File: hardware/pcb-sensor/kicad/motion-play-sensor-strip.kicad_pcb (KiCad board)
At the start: 2 copper layers, 69.8 x 10 mm, 9 parts, among them J1 Power In, J2 Power Out, J3 I2C+INT, U1 VCNL4040M3OE-H3

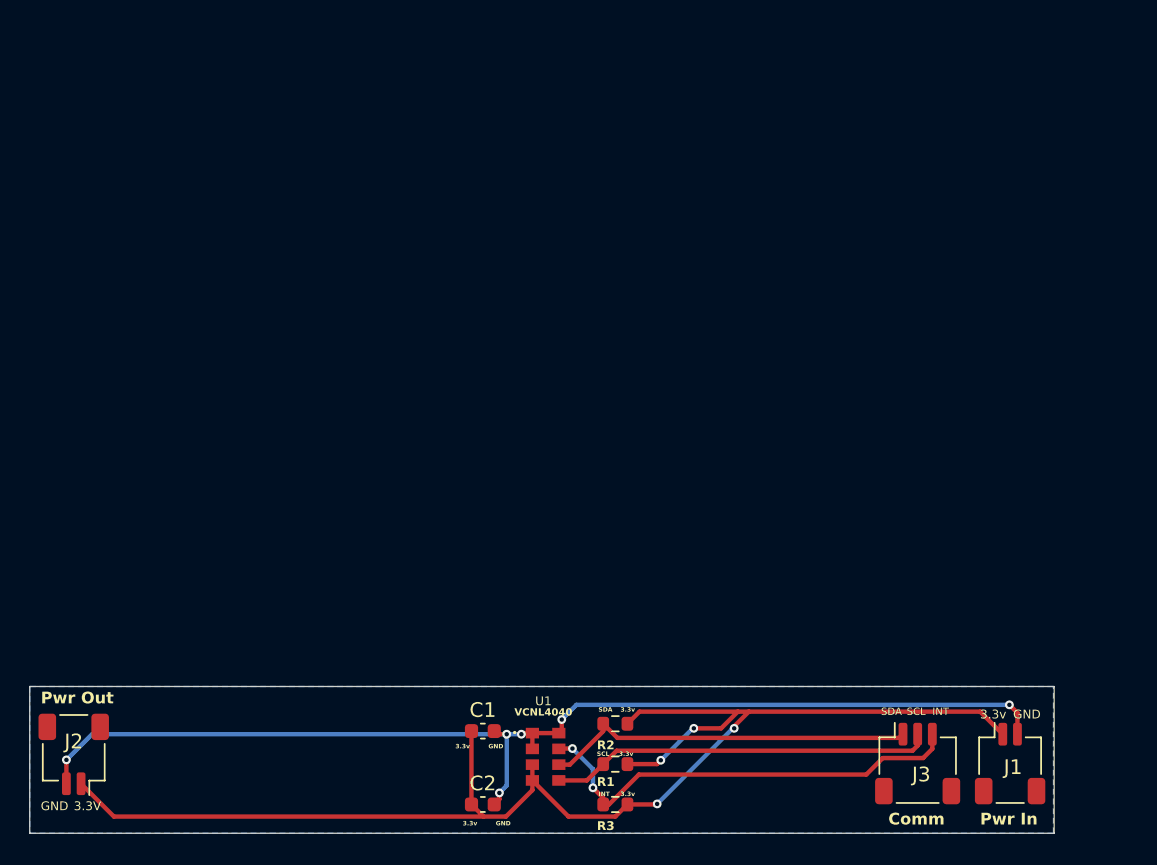
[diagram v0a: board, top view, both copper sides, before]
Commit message: Finished sensor redesign
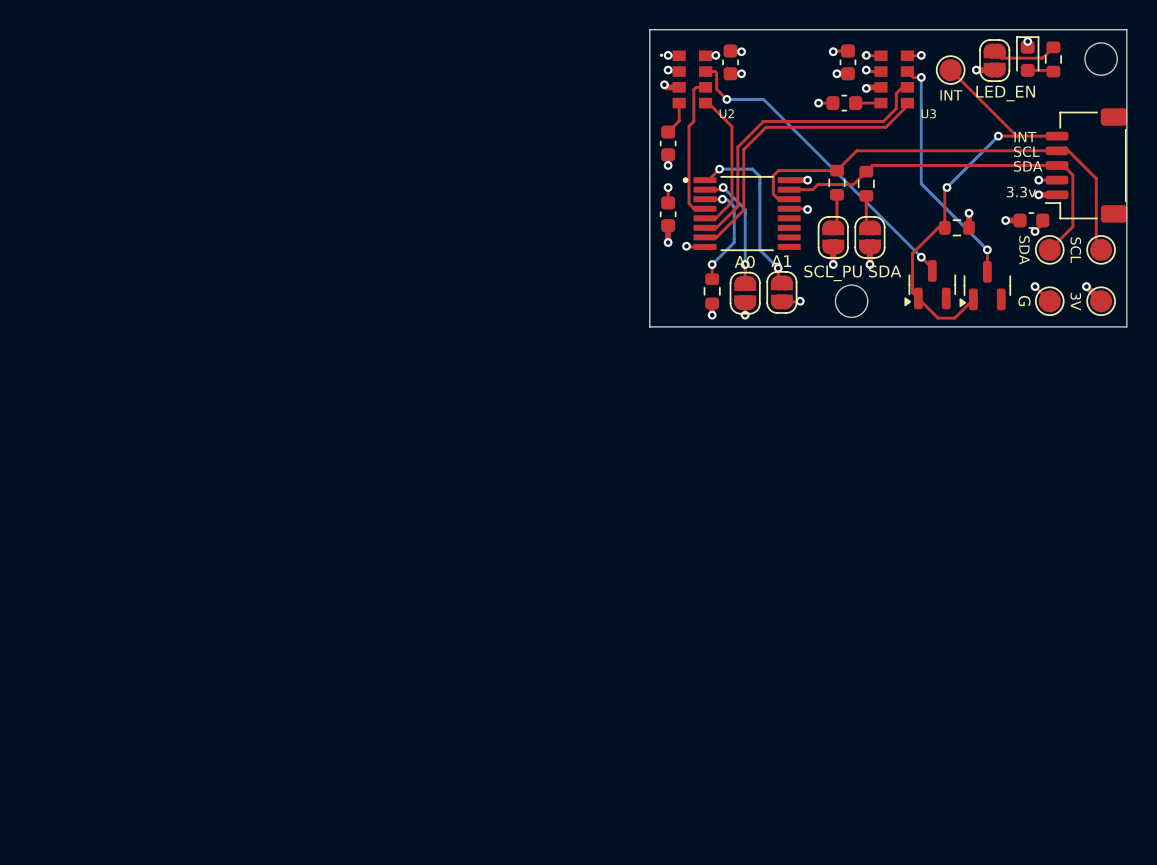
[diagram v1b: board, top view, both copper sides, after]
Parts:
- removed J2: Power Out, Connector_JST:JST_SH_SM02B-SRSS-TB_1x02-1MP_P1.00mm_Horizontal
- removed J3: I2C+INT, Connector_JST:JST_SH_SM03B-SRSS-TB_1x03-1MP_P1.00mm_Horizontal
- added C3: 2.2µF, Capacitor_SMD:C_0603_1608Metric, F.Cu at (143.5, 56.0)
- added C4: 2.2µF, Capacitor_SMD:C_0603_1608Metric, F.Cu at (155.5, 53.2)
- added C5: 0.1µF, Capacitor_SMD:C_0603_1608Metric, F.Cu at (155.8, 50.5)
- added C6: 0.1µF, Capacitor_SMD:C_0603_1608Metric, F.Cu at (143.5, 60.8)
- added D1: LED, LED_SMD:LED_0603_1608Metric, F.Cu at (168.0, 50.2)
- added D2: BAT54S, Package_TO_SOT_SMD:SOT-23, F.Cu at (161.5, 65.6)
- added D3: BAT54S, Package_TO_SOT_SMD:SOT-23, F.Cu at (165.2, 65.7)
- added JP1: SolderJumper_2_Open, Jumper:SolderJumper-2_P1.3mm_Open_RoundedPad1.0x1.5mm, F.Cu at (157.2, 62.4)
- added JP2: SolderJumper_2_Open, Jumper:SolderJumper-2_P1.3mm_Open_RoundedPad1.0x1.5mm, F.Cu at (154.8, 62.4)
- added JP3: SolderJumper_2_Open, Jumper:SolderJumper-2_P1.3mm_Open_RoundedPad1.0x1.5mm, F.Cu at (148.8, 66.2)
- added JP4: SolderJumper_2_Open, Jumper:SolderJumper-2_P1.3mm_Open_RoundedPad1.0x1.5mm, F.Cu at (151.2, 66.2)
- added JP5: SolderJumper_2_Open, Jumper:SolderJumper-2_P1.3mm_Open_RoundedPad1.0x1.5mm, F.Cu at (165.8, 50.4)
- added R4: 1kΩ, Resistor_SMD:R_0603_1608Metric, F.Cu at (169.8, 50.3)
- added R5: 10kΩ, Resistor_SMD:R_0603_1608Metric, F.Cu at (163.2, 61.8)
- added REF**: MountingHole_2.2mm_M2, MountingHole:MountingHole_2.2mm_M2, F.Cu at (173.0, 50.2)
- added REF**: MountingHole_2.2mm_M2, MountingHole:MountingHole_2.2mm_M2, F.Cu at (156.0, 66.8)
- added TP1: TestPoint_Small, TestPoint:TestPoint_Pad_D1.5mm, F.Cu at (173.0, 66.8)
- added TP2: TestPoint_Small, TestPoint:TestPoint_Pad_D1.5mm, F.Cu at (169.5, 66.8)
- added TP3: TestPoint_Small, TestPoint:TestPoint_Pad_D1.5mm, F.Cu at (169.5, 63.2)
- added TP4: TestPoint_Small, TestPoint:TestPoint_Pad_D1.5mm, F.Cu at (173.0, 63.2)
- added TP5: TestPoint_Small, TestPoint:TestPoint_Pad_D1.5mm, F.Cu at (162.8, 51.0)
- added U2: VCNL4040M3OE-H3, motion-play-footprints:VISHAY_VCNL4040, F.Cu at (145.2, 51.6)
- added U3: VCNL4040M3OE-H3, motion-play-footprints:VISHAY_VCNL4040, F.Cu at (158.9, 51.6)
- C1: value 100nF -> 2.2µF
- C2: value 2.2μF -> 0.1µF
- J1: value Power In -> Conn_01x05; footprint Connector_JST:JST_SH_SM02B-SRSS-TB_1x02-1MP_P1.00mm_Horizontal -> Connector_JST:JST_SH_SM05B-SRSS-TB_1x05-1MP_P1.00mm_Horizontal
- R1, R2: value 2.2kΩ -> 4.7kΩ
- R3: value 8.2kΩ -> 10kΩ
- U1: value VCNL4040M3OE-H3 -> PCA9546APWR; footprint VCNL4040:VISHAY_VCNL4040 -> motion-play-footprints:SOP65P640X120-16N
- moved C2 53.3 mm to (147.8, 50.5), turned to -90 degrees
- moved C1 51.1 mm to (168.2, 61.2), turned to 180 degrees
- moved R1 43.1 mm to (157.0, 58.8), turned to 90 degrees
- moved J1 41.1 mm to (172.0, 57.5), turned to 90 degrees
- moved R2 39.8 mm to (155.0, 58.7), turned to 90 degrees
- moved U1 39.5 mm to (148.9, 60.8)
- moved R3 35.6 mm to (146.5, 66.1), turned to -90 degrees
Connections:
- C1 pad 1: +3.3V -> GND
- C1 pad 2: GND -> +3.3V
- C2 pad 1: +3.3V -> GND
- C2 pad 2: GND -> +3.3V
- R1 pad 1: +3.3V -> Net-(JP1-B)
- R1 pad 2: /SCL -> Net-(J1-Pin_3)
- R2 pad 1: +3.3V -> Net-(JP2-B)
- R2 pad 2: /SDA -> Net-(J1-Pin_4)
- R3 pad 1: +3.3V -> Net-(U1-~{RESET})
- R3 pad 2: Net-(J3-Pin_3) -> +3.3V
- U1 pad 1: GND -> Net-(JP4-A)
- U1 pad 2: GND -> Net-(JP3-A)
- U1 pad 3: +3.3V -> Net-(U1-~{RESET})
- U1 pad 4: +3.3V -> Net-(U1-SD0)
- U1 pad 5: /SCL -> Net-(U1-SC0)
- U1 pad 6: /SDA -> Net-(U1-SD1)
- U1 pad 7: Net-(J3-Pin_3) -> Net-(U1-SC1)
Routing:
- net +3.3V: track 94.7 -> 15.1 mm, vias 4 -> 14
- net GND: track 77.2 -> 18.4 mm, vias 6 -> 19
- net Net-(J1-Pin_4): track 0.00 -> 31.0 mm
- net Net-(J3-Pin_3): track 30.6 -> 0.00 mm, vias 2 -> 0
- net Net-(D2-A): track 0.00 -> 29.1 mm, vias 0 -> 2
- net /SCL: track 26.2 -> 0.00 mm
- net Net-(J1-Pin_3): track 0.00 -> 26.0 mm
- net /SDA: track 25.4 -> 0.00 mm
- net Net-(D2-COM): track 0.00 -> 21.8 mm, vias 0 -> 2
- net Net-(U1-SD1): track 0.00 -> 20.7 mm
- net Net-(U1-SC1): track 0.00 -> 20.1 mm
- net Net-(D3-COM): track 0.00 -> 16.2 mm, vias 0 -> 2
- net Net-(JP4-A): track 0.00 -> 12.1 mm, vias 0 -> 2
- net Net-(U1-SD0): track 0.00 -> 10.8 mm
- net Net-(U1-SC0): track 0.00 -> 9.91 mm
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- added copper zone on In2.Cu, net +3.3V
- added copper zone on In1.Cu, net GND
- removed copper zone on B.Cu, net GND
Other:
- board size 69.8 x 10 mm -> 32.5 x 20.2 mm
- copper layers 2 -> 4
- board text removed: "3.3V"
- board text removed: "Comm"
- board text removed: "GND"
- board text removed: "Pwr In"
- board text removed: "Pwr Out"
- board text removed: "VCNL4040"
